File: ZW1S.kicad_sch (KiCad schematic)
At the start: 0 parts

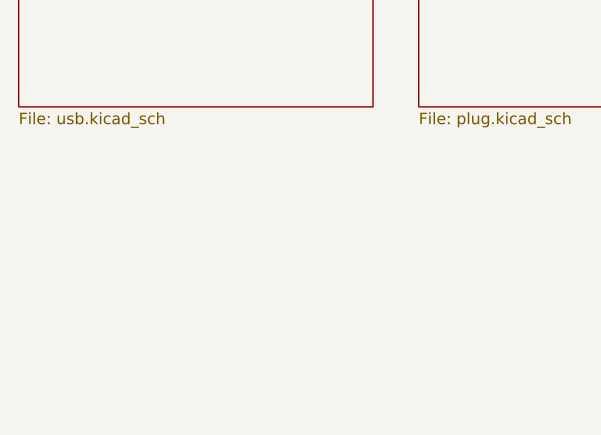
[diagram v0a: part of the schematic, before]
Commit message: 暂存: 基本完成原理图(未分配封装，未ERC)
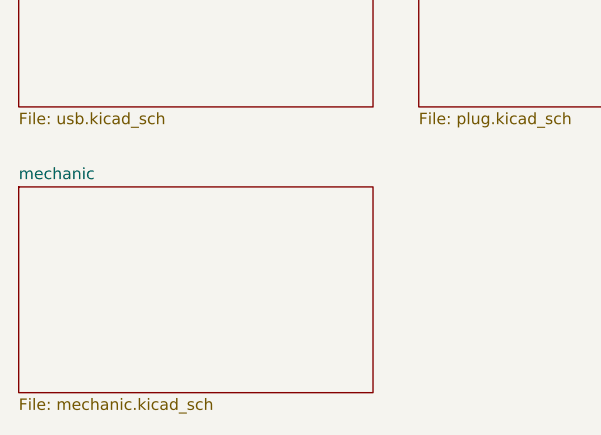
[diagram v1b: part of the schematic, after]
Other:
- added sheet mechanic (mechanic.kicad_sch)
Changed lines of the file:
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@@
 	(paper "A4")
+	(sheet
+		(at 30.48 156.21)
+		(size 39.37 22.86)
+		(fields_autoplaced yes)
+		(stroke
+			(width 0.1524)
+			(type solid)
+		)
+		(fill
+			(color 255 255 194 1.0000)
+		)
+		(property "Sheetname" "mechanic"
+			(at 30.48 155.4984 0)
+			(effects
+				(font
+					(size 1.27 1.27)
+				)
+				(justify left bottom)
+			)
+		)
+		(property "Sheetfile" "mechanic.kicad_sch"
+			(at 30.48 179.6546 0)
+			(effects
+				(font
+					(size 1.27 1.27)
+				)
+				(justify left top)
+			)
+		)
+		(instances
+			(project "ZW1S"
+				(path "/c658c753-a869-4eb9-a520-6b2e7fae7fd9"
+					(page "7")
+				)
+			)
+		)
+	)
 	(sheet
 		(at 74.93 92.71)

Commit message: 暂存: 基本完成原理图(差雷达接口)
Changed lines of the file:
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@@
 	(paper "A4")
 	(sheet
-		(at 30.48 156.21)
+		(at 63.5 110.49)
 		(size 39.37 22.86)
 		(fields_autoplaced yes)
@@
 		)
 		(property "Sheetname" "mechanic"
-			(at 30.48 155.4984 0)
+			(at 63.5 109.7784 0)
 			(effects
 				(font
@@
 		)
 		(property "Sheetfile" "mechanic.kicad_sch"
-			(at 30.48 179.6546 0)
+			(at 63.5 133.9346 0)
 			(effects
 				(font
@@
 	)
 	(sheet
-		(at 74.93 92.71)
+		(at 107.95 46.99)
 		(size 39.37 22.86)
 		(fields_autoplaced yes)
@@
 		)
 		(property "Sheetname" "power"
-			(at 74.93 91.9984 0)
+			(at 107.95 46.2784 0)
 			(effects
 				(font
@@
 		)
 		(property "Sheetfile" "power.kicad_sch"
-			(at 74.93 116.1546 0)
+			(at 107.95 70.4346 0)
 			(effects
 				(font
@@
 	)
 	(sheet
-		(at 30.48 92.71)
+		(at 63.5 46.99)
 		(size 39.37 22.86)
 		(fields_autoplaced yes)
@@
 		)
 		(property "Sheetname" "mcu"
-			(at 30.48 91.9984 0)
+			(at 63.5 46.2784 0)
 			(effects
 				(font
@@
 		)
 		(property "Sheetfile" "mcu.kicad_sch"
-			(at 30.48 116.1546 0)
+			(at 63.5 70.4346 0)
 			(effects
 				(font
@@
 	)
 	(sheet
-		(at 30.48 124.46)
+		(at 63.5 78.74)
 		(size 39.37 22.86)
 		(fields_autoplaced yes)
@@
 		)
 		(property "Sheetname" "usb"
-			(at 30.48 123.7484 0)
+			(at 63.5 78.0284 0)
 			(effects
 				(font
@@
 		)
 		(property "Sheetfile" "usb.kicad_sch"
-			(at 30.48 147.9046 0)
+			(at 63.5 102.1846 0)
 			(effects
 				(font
@@
 	)
 	(sheet
-		(at 74.93 124.46)
+		(at 107.95 78.74)
 		(size 39.37 22.86)
 		(fields_autoplaced yes)
@@
 		)
 		(property "Sheetname" "plug"
-			(at 74.93 123.7484 0)
+			(at 107.95 78.0284 0)
 			(effects
 				(font
@@
 		)
 		(property "Sheetfile" "plug.kicad_sch"
-			(at 74.93 147.9046 0)
+			(at 107.95 102.1846 0)
 			(effects
 				(font
